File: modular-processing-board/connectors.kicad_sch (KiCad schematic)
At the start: 3 parts

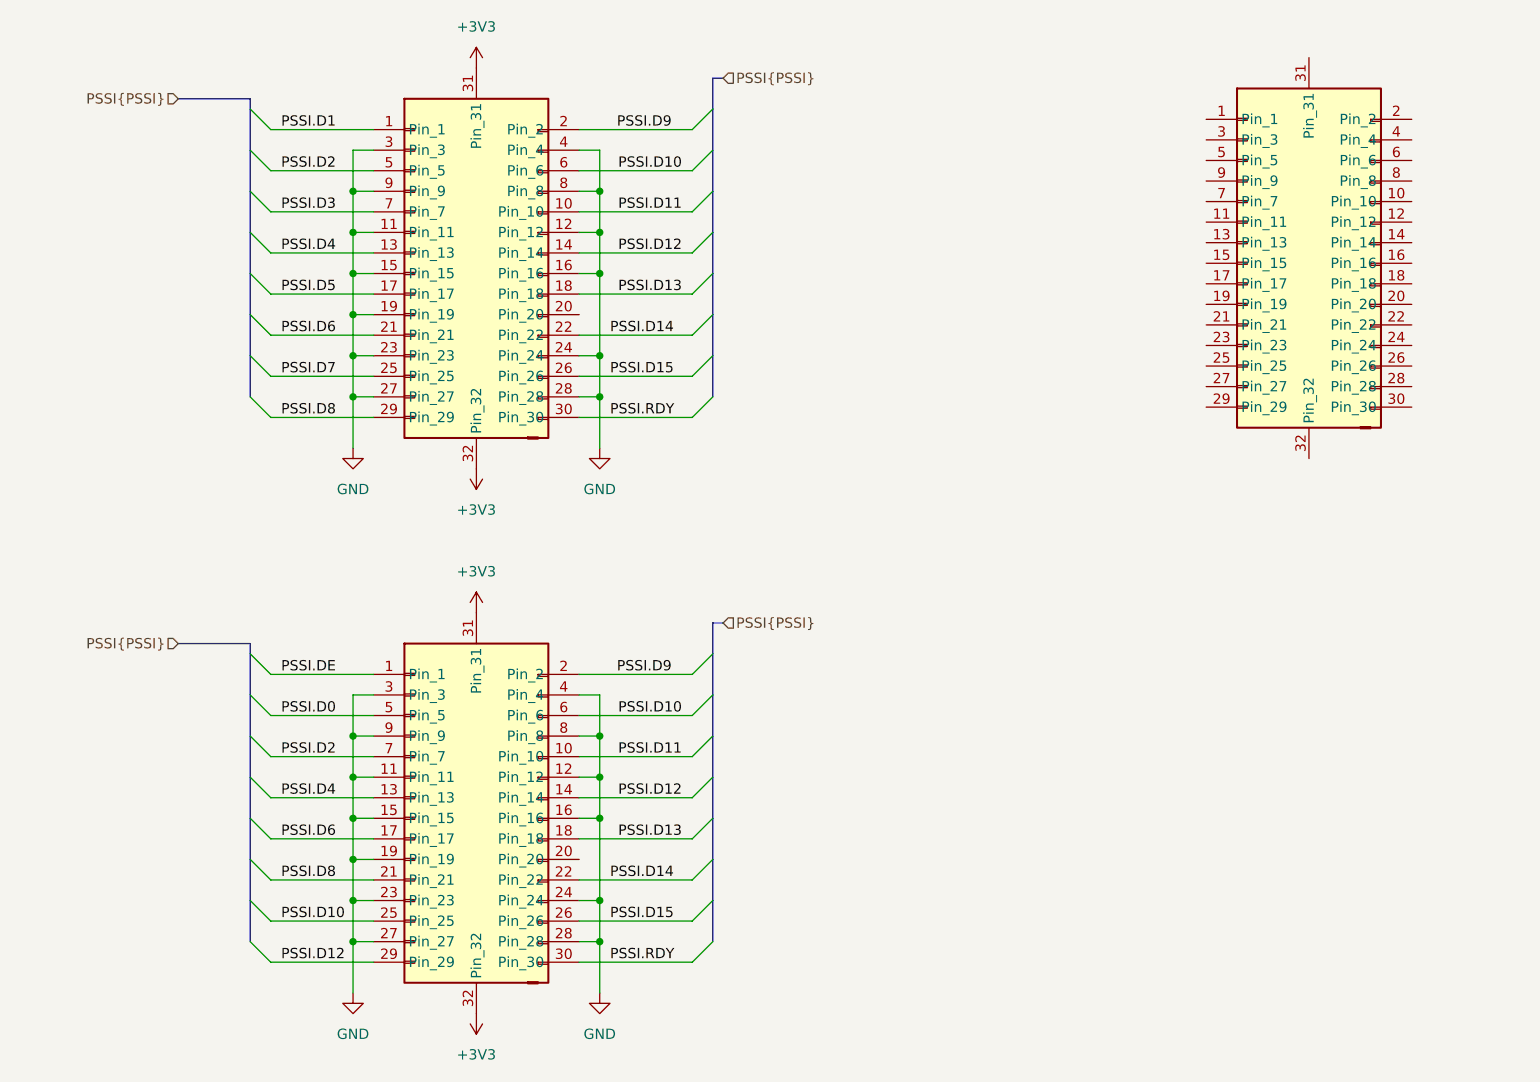
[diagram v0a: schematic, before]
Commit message: decided on fully differential configuratinon with ths4521 for both ADC inputs
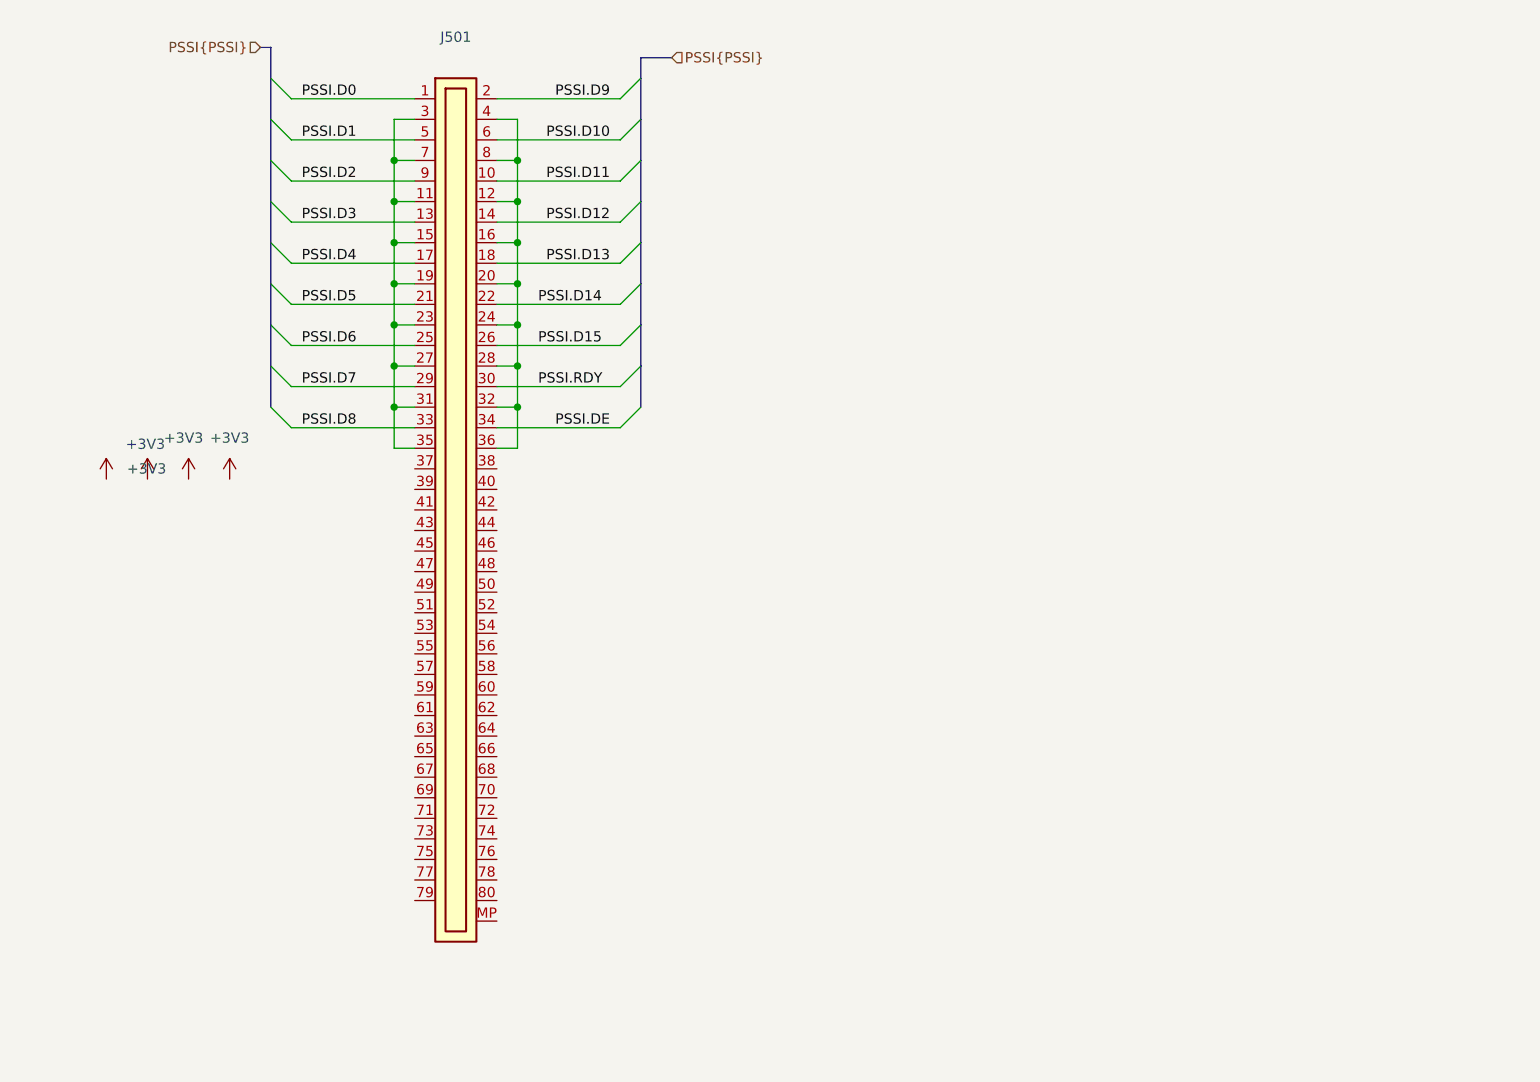
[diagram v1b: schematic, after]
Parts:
- removed U101, U501, U502: ~, iw-connector:Hirose_BM28-BM28B0.6-30DP-2-0.35V_2x10_P0.35mm_PowerPin2_Vertical, symbol iw-connector:BM28B0.6-30DP/2-0.35V
- added J501: Plug_Hirose_DF40_2x40_DF40C-80DP-0.4V, iw-connector:HRS_DF40C-80DP-0.4V(51), symbol iw-connector:Plug_Hirose_DF40_2x40_DF40C-80DP-0.4V
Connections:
- net PSSI.D0: now also J501.1
- net PSSI.D1: now also J501.5
- net PSSI.D10: now also J501.6
- net PSSI.D11: now also J501.10
- net PSSI.D12: now also J501.14
- net PSSI.D13: now also J501.18
- net PSSI.D14: now also J501.22
- net PSSI.D15: now also J501.26
- net PSSI.D2: now also J501.9
- net PSSI.D3: now also J501.13
- net PSSI.D4: now also J501.17
- net PSSI.D5: now also J501.21
- net PSSI.D6: now also J501.25
- net PSSI.D7: now also J501.29
- net PSSI.D8: now also J501.33
- net PSSI.D9: now also J501.2
- net PSSI.DE: now also J501.34
- net PSSI.RDY: now also J501.30
- new net: J501.11, J501.15, J501.19, J501.23, J501.27, J501.3, J501.31, J501.35, J501.7
- new net: J501.12, J501.16, J501.20, J501.24, J501.28, J501.32, J501.36, J501.4, J501.8

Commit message: Finished basic HW (next) Fix-up all labeling, then start laying out
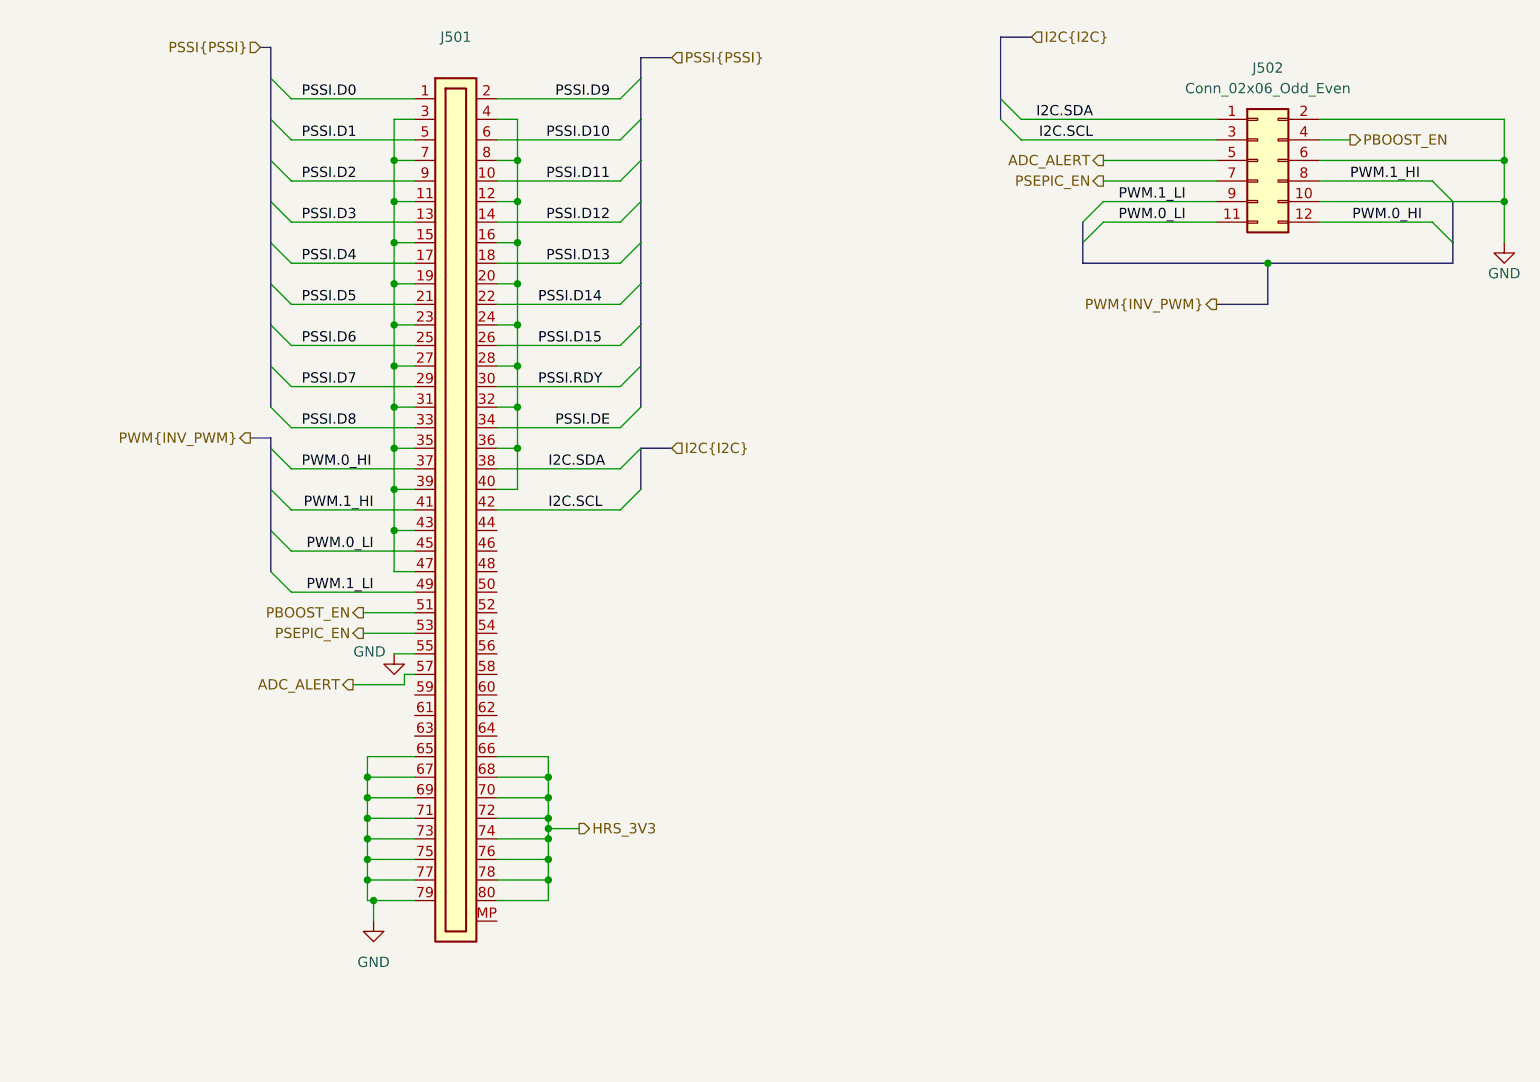
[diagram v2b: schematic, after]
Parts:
- added J502: Conn_02x06_Odd_Even, Connector_PinSocket_2.54mm:PinSocket_2x06_P2.54mm_Vertical, symbol Connector_Generic:Conn_02x06_Odd_Even
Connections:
- net at J501.11, J501.15, J501.19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: now also J501.39, J501.43, J501.47
- net at J501.12, J501.16, J501.20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: now also J501.40
- net PWM.0_HI: now reaches J501.37
- net PWM.0_HI: now also J502.12 (Pin_12)
- net I2C.SDA: now reaches J501.38
- net I2C.SDA: now also J502.1 (Pin_1)
- net PWM.1_HI: now reaches J501.41
- net PWM.1_HI: now also J502.8 (Pin_8)
- net I2C.SCL: now reaches J501.42
- net I2C.SCL: now also J502.3 (Pin_3)
- net PWM.0_LI: now reaches J501.45
- net PWM.0_LI: now also J502.11 (Pin_11)
- net PWM.1_LI: now reaches J501.49
- net PWM.1_LI: now also J502.9 (Pin_9)
- net PBOOST_EN: now reaches J501.51
- net PBOOST_EN: now also J502.4 (Pin_4)
- net PSEPIC_EN: now reaches J501.53
- net PSEPIC_EN: now also J502.7 (Pin_7)
- net GND: now reaches J501.55
- net GND: now also J501.65, J501.67, J501.69, J501.71, J501.73, J501.75, J501.77, J501.79, J502.10 (Pin_10), J502.2 (Pin_2), J502.6 (Pin_6)
- net ADC_ALERT: now reaches J501.57
- net ADC_ALERT: now also J502.5 (Pin_5)
- net HRS_3V3: now reaches J501.66
- net HRS_3V3: now also J501.68, J501.70, J501.72, J501.74, J501.76, J501.78, J501.80

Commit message: completed schematic
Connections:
- net GND: now also J501.MP
- net I2C.SCL: now also J501.46; no longer J501.42
- net I2C.SDA: now also J501.42; no longer J501.38
- net at J501.12, J501.16, J501.20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: now also J501.44, J501.48
- new net PSSI.PDCK: J501.38
- no-connect marks 0 -> 11
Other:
- note added: "Mounting Pin"

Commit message: rough length mamatching for sdram (next) route PSSI-bus
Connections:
- net GND: now also J501.11, J501.12, J501.15, J501.16, J501.19, J501.20, J501.23, J501.24, J501.27, J501.28, J501.3, J501.31, J501.32, J501.35, J501.36, J501.39, J501.4, J501.40, J501.43, J501.44, J501.47, J501.48, J501.7, J501.8
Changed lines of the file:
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@@
+	)
+	(junction
+		(at 67.31 109.22)
+		(diameter 0)
+		(color 0 0 0 0)
 	)
 	(junction
@@
 	(junction
 		(at 64.008 137.16)
+		(diameter 0)
+		(color 0 0 0 0)
+	)
+	(junction
+		(at 82.55 109.22)
 		(diameter 0)
 		(color 0 0 0 0)
@@
 	(symbol
 		(lib_id "power:GND")
+		(at 67.31 109.22 0)
+		(unit 1)
+		(exclude_from_sim no)
+		(in_bom yes)
+		(on_board yes)
+		(dnp no)
+		(fields_autoplaced yes)
+		(property "Reference" "#PWR0506"
+			(at 67.31 115.57 0)
+			(effects
+				(font
+					(size 1.27 1.27)
+				)
+				(hide yes)
+			)
+		)
+		(property "Value" "GND"
+			(at 67.31 114.3 0)
+			(effects
+				(font
+					(size 1.27 1.27)
+				)
+			)
+		)
+		(property "Footprint" ""
+			(at 67.31 109.22 0)
+			(effects
+				(font
+					(size 1.27 1.27)
+				)
+				(hide yes)
+			)
+		)
+		(property "Datasheet" ""
+			(at 67.31 109.22 0)
+			(effects
+				(font
+					(size 1.27 1.27)
+				)
+				(hide yes)
+			)
+		)
+		(property "Description" "Power symbol creates a global label with name \"GND\" , ground"
+			(at 67.31 109.22 0)
+			(effects
+				(font
+					(size 1.27 1.27)
+				)
+				(hide yes)
+			)
+		)
+		(pin "1"
+		)
+		(instances
+			(project "modular-processing-board"
+				(path "/73b5a92f-908b-4f97-a96c-14ee20a7f293/af568620-9ac5-4253-a292-c4ce6ef3e371"
+					(reference "#PWR0506")
+					(unit 1)
+				)
+			)
+		)
+	)
+	(symbol
+		(lib_id "power:GND")
 		(at 67.31 119.38 0)
 		(unit 1)
@@
 					(unit 1)
 				)
+			)
+		)
+	)
+	(symbol
+		(lib_id "power:GND")
+		(at 82.55 109.22 0)
+		(unit 1)
+		(exclude_from_sim no)
+		(in_bom yes)
+		(on_board yes)
+		(dnp no)
+		(fields_autoplaced yes)
+		(property "Reference" "#PWR0505"
+			(at 82.55 115.57 0)
+			(effects
+				(font
+					(size 1.27 1.27)
+				)
+				(hide yes)
+			)
+		)
+		(property "Value" "GND"
+			(at 82.55 114.3 0)
+			(effects
+				(font
+					(size 1.27 1.27)
+				)
+			)
+		)
+		(property "Footprint" ""
+			(at 82.55 109.22 0)
+			(effects
+				(font
+					(size 1.27 1.27)
+				)
+				(hide yes)
+			)
+		)
+		(property "Datasheet" ""
+			(at 82.55 109.22 0)
+			(effects
+				(font
+					(size 1.27 1.27)
+				)
+				(hide yes)
+			)
+		)
+		(property "Description" "Power symbol creates a global label with name \"GND\" , ground"
+			(at 82.55 109.22 0)
+			(effects
+				(font
+					(size 1.27 1.27)
+				)
+				(hide yes)
+			)
+		)
+		(pin "1"
+		)
+		(instances
+			(project ""
+				(path "/73b5a92f-908b-4f97-a96c-14ee20a7f293/af568620-9ac5-4253-a292-c4ce6ef3e371"
+					(reference "#PWR0505")
+					(unit 1)
+				)

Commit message: reconnected vref
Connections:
- net ADC_ALERT renamed AD_ALERT
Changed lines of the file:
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@@
 		)
 	)
-	(hierarchical_label "ADC_ALERT"
+	(hierarchical_label "AD_ALERT"
 		(shape output)
 		(at 154.94 58.42 180)
@@
 		)
 	)
-	(hierarchical_label "ADC_ALERT"
+	(hierarchical_label "AD_ALERT"
 		(shape output)
 		(at 62.23 123.19 180)

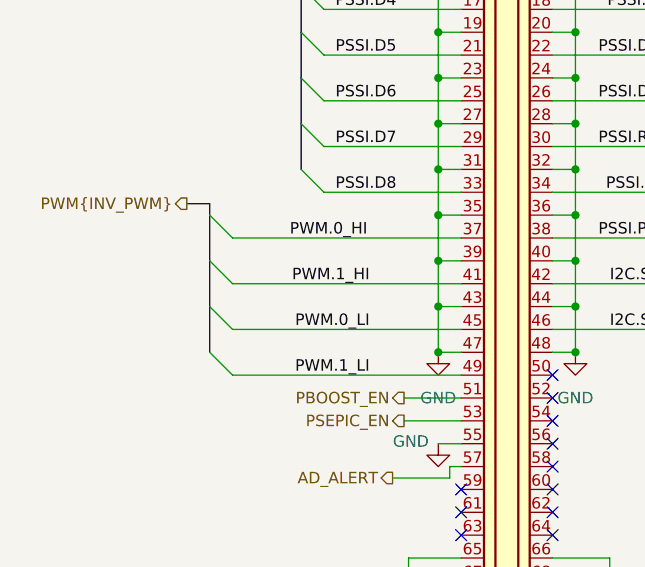
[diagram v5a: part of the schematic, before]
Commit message: finished schematic checks, added extra capacitors on LDO output (next) add holes to board / board shape, do layout checks
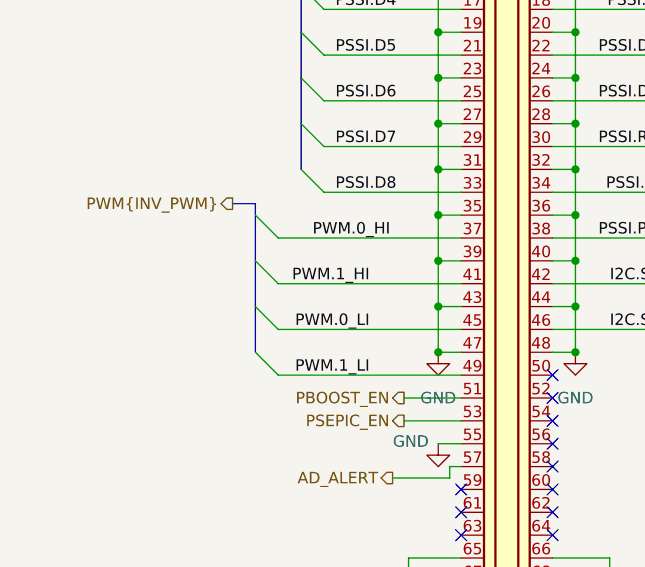
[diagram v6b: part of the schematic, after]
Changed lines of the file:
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@@
 	)
 	(bus_entry
-		(at 41.91 93.98)
+		(at 46.99 93.98)
 		(size 2.54 2.54)
 		(stroke
@@
 	)
 	(bus_entry
-		(at 44.45 111.76)
+		(at 49.53 111.76)
 		(size -2.54 -2.54)
 		(stroke
@@
 	)
 	(bus_entry
-		(at 41.91 104.14)
+		(at 46.99 104.14)
 		(size 2.54 2.54)
 		(stroke
@@
 	)
 	(bus_entry
-		(at 44.45 101.6)
+		(at 49.53 101.6)
 		(size -2.54 -2.54)
 		(stroke
@@
 	(wire
 		(pts
-			(xy 44.45 111.76) (xy 69.85 111.76)
-		)
-		(stroke
-			(width 0)
-			(type default)
-		)
-	)
-	(wire
-		(pts
 			(xy 67.31 78.74) (xy 67.31 83.82)
 		)
@@
 	(wire
 		(pts
+			(xy 49.53 111.76) (xy 69.85 111.76)
+		)
+		(stroke
+			(width 0)
+			(type default)
+		)
+	)
+	(wire
+		(pts
 			(xy 185.42 55.88) (xy 181.61 55.88)
 		)
@@
 	(wire
 		(pts
-			(xy 44.45 106.68) (xy 69.85 106.68)
+			(xy 49.53 106.68) (xy 69.85 106.68)
 		)
 		(stroke
@@
 	(wire
 		(pts
-			(xy 44.45 96.52) (xy 69.85 96.52)
+			(xy 49.53 96.52) (xy 69.85 96.52)
 		)
 		(stroke
@@
 	(bus
 		(pts
-			(xy 41.91 92.71) (xy 39.37 92.71)
+			(xy 46.99 92.71) (xy 44.45 92.71)
 		)
 		(stroke
@@
 	(wire
 		(pts
-			(xy 44.45 101.6) (xy 69.85 101.6)
+			(xy 49.53 101.6) (xy 69.85 101.6)
 		)
 		(stroke
@@
 	(bus
 		(pts
-			(xy 41.91 93.98) (xy 41.91 92.71)
+			(xy 46.99 93.98) (xy 46.99 92.71)
 		)
 		(stroke
@@
 	(bus
 		(pts
-			(xy 41.91 104.14) (xy 41.91 99.06)
+			(xy 46.99 104.14) (xy 46.99 99.06)
 		)
 		(stroke
@@
 	(bus
 		(pts
-			(xy 41.91 99.06) (xy 41.91 93.98)
+			(xy 46.99 99.06) (xy 46.99 93.98)
 		)
 		(stroke
@@
 	(bus
 		(pts
-			(xy 41.91 104.14) (xy 41.91 109.22)
+			(xy 46.99 104.14) (xy 46.99 109.22)
 		)
 		(stroke
@@
 	)
 	(label "PWM.0_HI"
-		(at 50.8 96.52 0)
+		(at 53.34 96.52 0)
 		(effects
 			(font
@@
 	(hierarchical_label "PWM{INV_PWM}"
 		(shape output)
-		(at 39.37 92.71 180)
-		(effects
-			(font
+		(at 44.45 92.71 180)
+		(effects
+			(font

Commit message: matched PSSI bus lenghts
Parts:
- J501: Manufacturer Hirose Electric -> (none)
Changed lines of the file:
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@@
-			)
-		)
-		(property "Manufacturer" "Hirose Electric"
-			(at 95.25 63.5 0)
-			(effects
-				(font
-					(size 1.27 1.27)
-					(thickness 0.15)
-				)
-				(justify left bottom)
-				(hide yes)
 			)
 		)

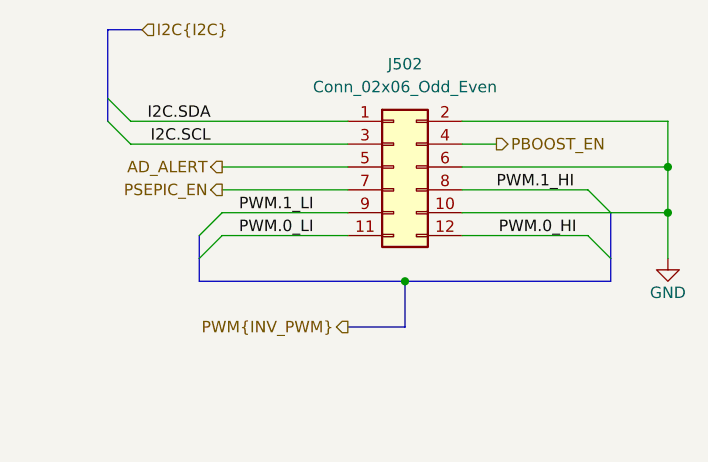
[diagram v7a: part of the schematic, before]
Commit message: minor changes in BOM and DNP-components
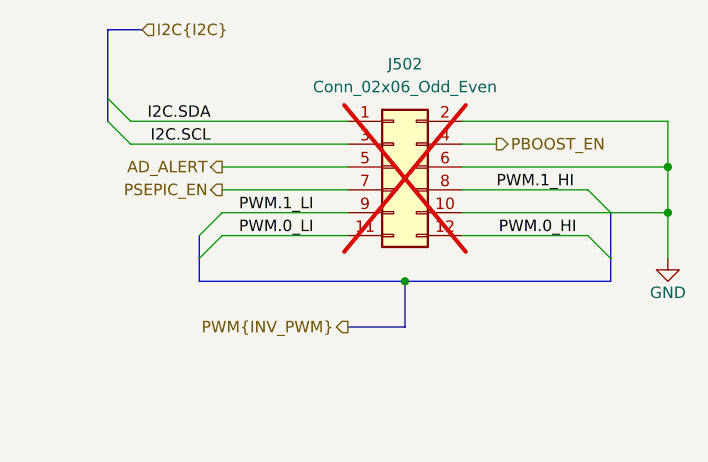
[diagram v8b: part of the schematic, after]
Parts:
- J502: now not fitted; now left out of the parts list
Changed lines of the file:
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@@
 		(unit 1)
 		(exclude_from_sim no)
-		(in_bom yes)
+		(in_bom no)
 		(on_board yes)
-		(dnp no)
+		(dnp yes)
 		(fields_autoplaced yes)
 		(property "Reference" "J502"
